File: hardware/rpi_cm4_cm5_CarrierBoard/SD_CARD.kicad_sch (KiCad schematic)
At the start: 17 parts, among them J1 DM3AT-SF-PEJM5, Q4 2N7002, Q5 2N7002, Q6 2N7002, U4 AP22913W6-7

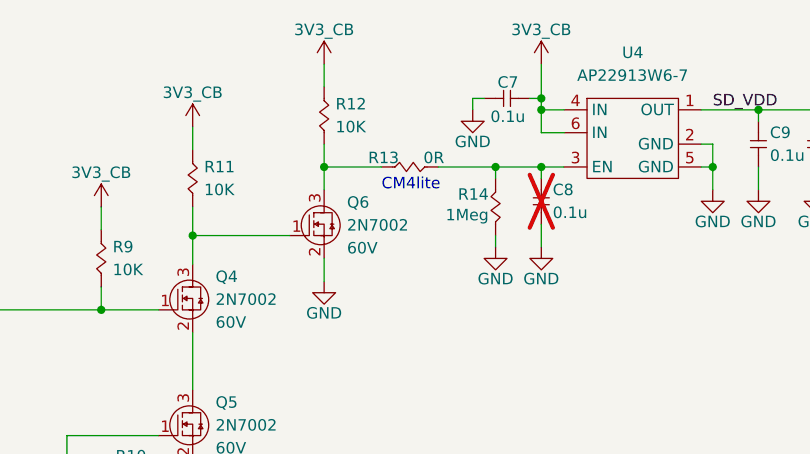
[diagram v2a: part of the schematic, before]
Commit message: Document stackup Few changes to schematic based on preliminary PCB placement Update PinMux based on preliminary PCB placement and component positions
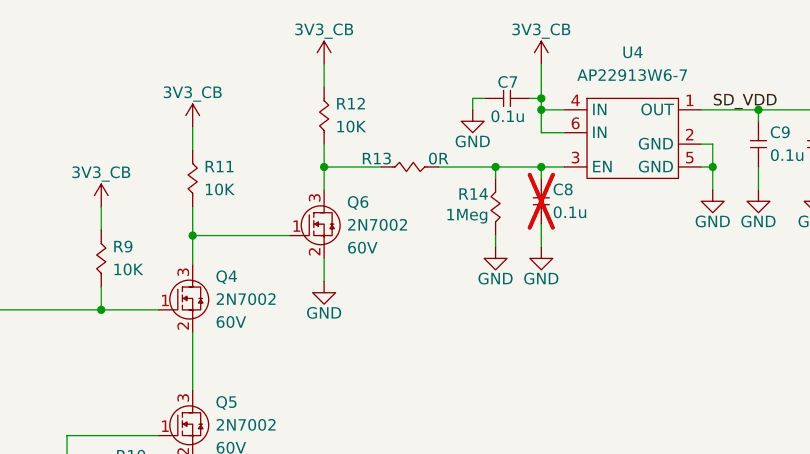
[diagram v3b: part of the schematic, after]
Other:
- note removed: "CM4lite"
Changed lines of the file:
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@@
 	(title_block
 		(title "RPI CMx Carrier")
-		(date "2025-12-07")
+		(date "2026-01-22")
 		(rev "2.00-0A")
 		(comment 1 "Jean-Francois Bilodeau")
@@
 	(bus_alias "SDIO"
 		(members "SDIO_D0" "SDIO_D1" "SDIO_D2" "SDIO_D3" "SDIO_CLK" "SDIO_CMD")
-	)
-	(text "CM4lite"
-		(exclude_from_sim no)
-		(at 112.522 62.357 0)
-		(effects
-			(font
-				(size 1.27 1.27)
-			)
-		)
 	)
 	(text "Resistors are 1% 1/16W 0402 unless otherwise noted\nCapacitors are 10% 50V X7R 0402 unless otherwise noted"
@@
 		(dnp no)
 		(property "Reference" "R13"
-			(at 109.474 59.309 0)
+			(at 108.712 59.436 0)
 			(effects
 				(font
@@
 		)
 		(property "Value" "0R"
-			(at 115.062 59.309 0)
-			(effects
-				(font
+			(at 115.57 59.436 0)
+			(effects
+				(font
